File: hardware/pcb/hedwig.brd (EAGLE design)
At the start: 76.2 x 68.5 mm, 75 parts, among them IC1 MPL3115A2LGA, J1 DX07B024JJ1R1500, P1 JTAG-10MINI, Q1 16MHz, Q2 IRLML6402, U1 NRF24L01SMD, U2 TEXAS_INSTRUMENTS_TLC59731DRT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, U3 FT232RQ, U5 ADP2302, U7 9DoF IMU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

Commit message: updated schematic and pcb
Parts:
- removed U$6: DIODE, falcon:SMB
- removed U7: 9DoF IMU, SparkFun-Sensors:QFN24-3X3
- added 1.8V: TPB2,54, testpad:B2,54
- added C22: 47uF, SparkFun-Capacitors:0603@1
- added D3: SURS8360BT3G, falcon:SMB
- added Q3, Q6: 20V/0.2A/8MHz/1.2Ω/1Vth, SparkFun-DiscreteSemi:SOT-416FL
- added R11, R8: 5.1k, SparkFun-Resistors:0603
- added R12, R14: 2.49k, SparkFun-Resistors:0603
- added U4: TPS7A26-1.8, falcon:WSON
- added U6: 9DoF IMU, SparkFun-Sensors:QFN24-3X3
- C10, C11: value 1.5pF -> 0.1uF
- C14: value 2.2uF -> 0.1uF
- C17: value 100nF -> 0.1uF
- C18, C19, C20, C21: device SparkFun-Capacitors:0603 -> SparkFun-Capacitors:0603@1
- C8, C9: value 8.2pF -> 0.1uF
- moved C16 63.1 mm to (45.9, 58.3), turned to 270 degrees
- moved C20 51.4 mm to (3.00, 9.00), turned to 0 degrees
- moved 5V 30.2 mm to (23.0, 13.4)
- moved Q2 12.3 mm to (17.0, 14.0)
- moved R10 10.7 mm to (28.0, 15.0)
- moved C12 8.54 mm to (65.9, 45.8)
- moved C15 8.54 mm to (63.9, 51.3)
- moved IC1 8.54 mm to (71.5, 47.5)
- moved C21 8.45 mm to (3.00, 12.0)
- moved C5 8.32 mm to (24.1, 53.5)
- moved U$4 7.70 mm to (45.0, 16.0)
- moved R7 7.25 mm to (34.0, 8.00), turned to 90 degrees
- moved R5 7.00 mm to (29.6, 60.3)
- moved R6 7.00 mm to (31.8, 60.3)
- moved U5 5.91 mm to (36.0, 19.0)
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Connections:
- new net 1P8V: 1.8V.TP, C16.1, Q3.1, Q6.1, R12.2, R14.2, U4.1, U6.13, U6.22
- new net N$15: J1.B5, R8.2
- new net N$26: J1.A5, R11.2
- new net SENSOR_SCL_LV: Q6.2, R14.1, U6.23
- new net SENSOR_SDA_LV: Q3.2, R12.1, U6.24
- net +3V3: now also C22.1, U4.4, U4.6; no longer C16.1, U7.13, U7.22
- net +5V: now also D3.@2; no longer U$6.@2
- net ADSD_STUB: now also U6.9; no longer U7.9
- net GND: now also C22.2, R11.1, R8.1, U4.3, U4.5, U6.18, U6.20; no longer U7.18, U7.20
- net REGOUT: now also U6.10; no longer U7.10
- net SENSOR_SCL: now also Q6.3; no longer U7.23
- net SENSOR_SDA: now also Q3.3; no longer U7.24
- net USB_VCC: now also D3.@1; no longer U$6.@1
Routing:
- net 1P8V: track 0.00 -> 53.5 mm
- net SENSOR_SCL: track 47.6 -> 80.5 mm, vias 0 -> 2
- net +5V: track 72.1 -> 39.6 mm, vias 2 -> 0
- net SENSOR_SDA_LV: track 0.00 -> 29.0 mm
- net SENSOR_SCL_LV: track 0.00 -> 27.4 mm, vias 0 -> 2
- net SENSOR_SDA: track 50.4 -> 76.6 mm
- net N$15: track 0.00 -> 11.1 mm
- net N$25: track 28.1 -> 18.4 mm
- net N$26: track 0.00 -> 8.13 mm
- net GND: track 129.4 -> 137.1 mm, vias 50 -> 67
- net N$16: track 14.0 -> 21.0 mm
- net +3V3: track 65.7 -> 60.2 mm, vias 7 -> 9
- net N$23: track 5.08 -> 8.44 mm
- net N$22: track 12.5 -> 15.1 mm
- net N$21: track 12.5 -> 15.0 mm
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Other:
- board size 76.2 x 68.5 mm -> 78 x 70 mm
- board text added: "FALCON 1.1"

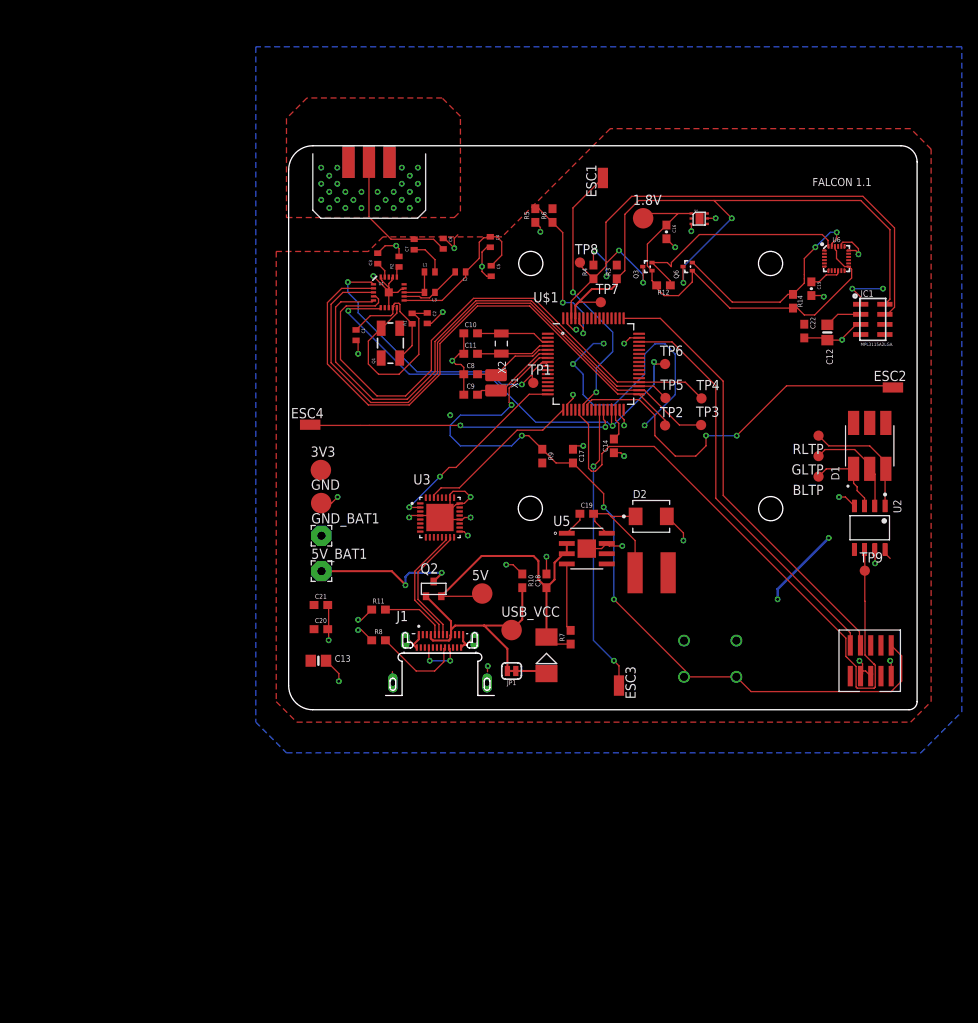
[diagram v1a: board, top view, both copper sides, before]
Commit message: change top plane to gnd and add breakout
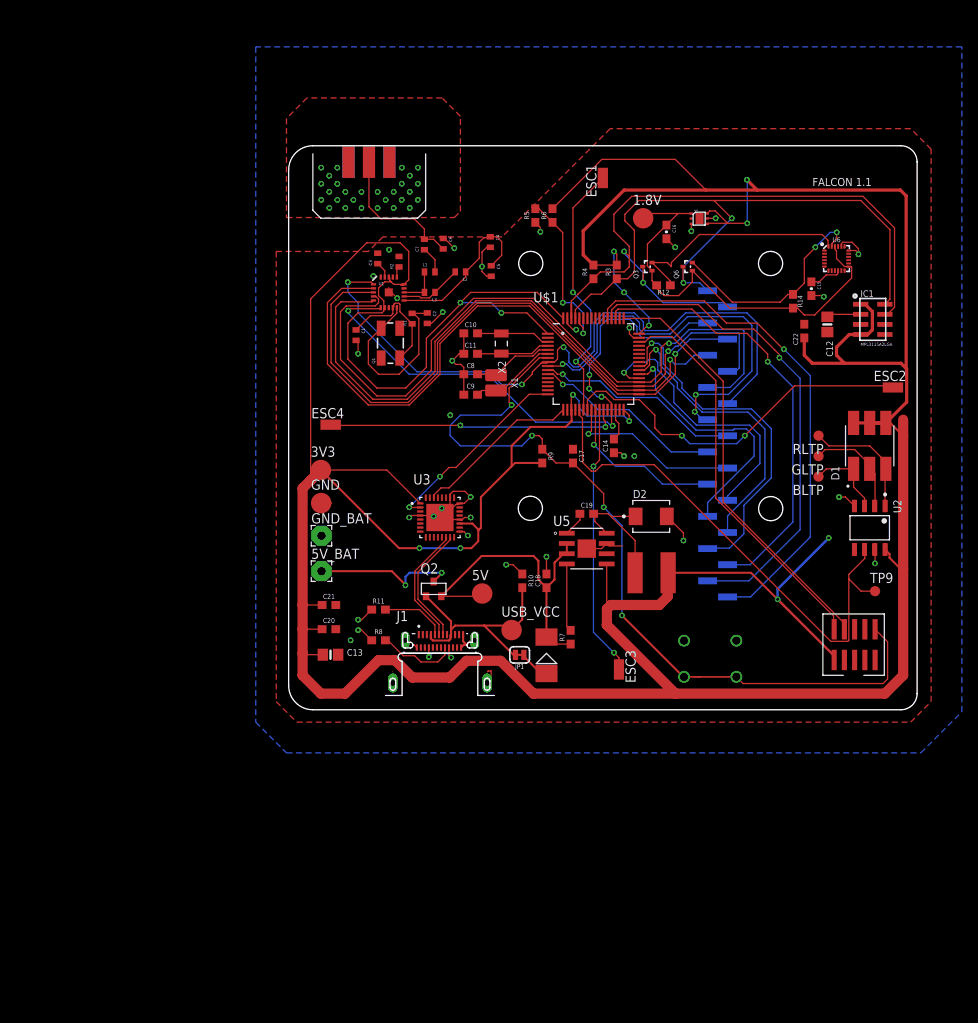
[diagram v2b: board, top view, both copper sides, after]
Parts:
- removed TP1, TP2, TP3, TP4, TP5, TP6, TP7, TP8: TPB1,27, testpad:B1,27
- added P2: SENSOR_SCL, falcon:STAGGERED-CONNECTOR
- added P3: RF_SCK, falcon:STAGGERED-CONNECTOR
- added P4: PC1, falcon:STAGGERED-CONNECTOR
- added P5: PC5, falcon:STAGGERED-CONNECTOR
- added P6: PC9, falcon:STAGGERED-CONNECTOR
- moved TP9 2.84 mm to (71.8, 13.7)
- moved P1 2.83 mm to (69.1, 7.08)
- moved ESC4 2.54 mm to (4.21, 34.4)
- moved JP1 2.24 mm to (27.7, 5.81)
- moved ESC3 2.00 mm to (40.0, 4.00)
- moved C13 1.68 mm to (4.19, 5.83)
- moved C7 1.27 mm to (15.8, 56.7)
- moved C12 1.00 mm to (65.9, 46.8)
- moved C20 1.00 mm to (4.00, 9.00)
- moved C21 1.00 mm to (4.00, 12.0)
- turned C22 to 90 degrees
- renumbered 5V_BAT1 to 5V_BAT, GND_BAT1 to GND_BAT
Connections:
- new net PC1: P4.1, U$1.9
- new net PC10: P6.2, U$1.51
- new net PC11: P6.3, U$1.52
- new net PC12: P6.4, U$1.53
- new net PC13: U$1.2
- new net PC2: P4.2, U$1.10
- new net PC3: P4.3, U$1.11
- new net PC4: P4.4, U$1.24
- new net PC5: P5.1, U$1.25
- new net PC6: P5.2, U$1.37
- new net PC7: P5.3, U$1.38
- new net PC8: P5.4, U$1.39
- new net PC9: P6.1, U$1.40
- net RF_CE: now also P3.4; no longer TP1.TP
- net RF_IRQ: now also P2.3; no longer TP6.TP
- net RF_MISO: now also P3.2; no longer TP5.TP
- net RF_MOSI: now also P3.3; no longer TP4.TP
- net RF_SCK: now also P3.1; no longer TP3.TP
- net RF_SS: now also P2.4; no longer TP2.TP
- net SENSOR_SCL: now also P2.1; no longer TP7.TP
- net SENSOR_SDA: now also P2.2; no longer TP8.TP
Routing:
- net +3V3: track 60.2 -> 579.1 mm, vias 9 -> 13
- net PC12: track 0.00 -> 64.0 mm, vias 0 -> 1
- net PC11: track 0.00 -> 61.8 mm, vias 0 -> 1
- net PC10: track 0.00 -> 54.6 mm, vias 0 -> 1
- net PC1: track 0.00 -> 51.7 mm, vias 0 -> 3
- net RF_CE: track 37.3 -> 84.5 mm, vias 2 -> 3
- net PC9: track 0.00 -> 44.4 mm, vias 0 -> 1
- net GND: track 137.1 -> 93.9 mm, vias 67 -> 61
- net PC8: track 0.00 -> 37.6 mm, vias 0 -> 1
- net PC6: track 0.00 -> 35.1 mm, vias 0 -> 1
- net PC7: track 0.00 -> 31.7 mm, vias 0 -> 1
- net PC2: track 0.00 -> 25.7 mm, vias 0 -> 1
- net PC3: track 0.00 -> 23.9 mm, vias 0 -> 1
- net PC4: track 0.00 -> 22.2 mm, vias 0 -> 1
- net PC5: track 0.00 -> 20.6 mm, vias 0 -> 1
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- removed copper zone on layer 1, net +3V3
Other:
- outline, holes or cut-outs redrawn
- board text added: "PC1"
- board text added: "PC11"
- board text added: "PC3"
- board text added: "PC5"
- board text added: "PC7"
- board text added: "PC9"
- board text added: "RF_IRQ"
- board text added: "RF_MOSI"
- board text added: "RF_SCK"
- board text added: "SENSOR_SCL"

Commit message: newest version - done
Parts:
- added C23: 47uF, SparkFun-Capacitors:0603@1
- added C24, C25: 0.1uF, SparkFun-Capacitors:0603@1
- added C26, C27, C28: 0.1uF, SparkFun-Capacitors:0603
- moved C13 73.1 mm to (68.7, 40.3), turned to 180 degrees
- moved C20 46.4 mm to (50.1, 14.4)
- moved C21 46.4 mm to (50.1, 17.4)
- moved C16 24.7 mm to (70.3, 54.9), turned to 90 degrees
- moved C22 16.2 mm to (52.1, 58.0), turned to 180 degrees
- moved C17 2.95 mm to (31.3, 30.4)
- moved R9 2.13 mm to (28.3, 30.5)
- moved ESC2 0.42 mm to (73.6, 39.1)
- renumbered IC1 to U7
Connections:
- removed net 1P8V: 1.8V.TP, C16.1, Q3.1, Q6.1, R12.2, R14.2, U4.1, U6.13, U6.22
- new net 1V8: 1.8V.TP, C16.1, C23.1, Q3.1, Q6.1, R12.2, R14.2, U4.1, U6.13, U6.22, U6.8
- net +3V3: now also C24.1, C25.1, C26.2, C27.2, C28.2
- net GND: now also C23.2, C24.2, C25.2, C26.1, C27.1, C28.1
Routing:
- net 1V8: track 0.00 -> 65.1 mm
- net 1P8V: track 53.7 -> 0.00 mm
- net GND: track 93.9 -> 86.2 mm, vias 61 -> 103
- net +3V3: track 579.1 -> 584.5 mm
- net SENSOR_SDA_LV: track 29.0 -> 28.3 mm
- net SWCLK: track 52.6 -> 53.2 mm
- net N$13: track 9.21 -> 9.81 mm
- net MOTOR2: track 46.3 -> 45.7 mm
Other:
- board text added: "/Users/adambujak/Workspace/FALCON/resources/tail.bmp"
- board text added: "PC10"
- board text added: "PC12"
- board text added: "PC2"
- board text added: "PC4"
- board text added: "PC6"
- board text added: "PC8"
- board text added: "RF_CE"
- board text added: "RF_MISO"
- board text added: "RF_SS"
- board text added: "SENSOR_SDA"
- board text removed: "FALCON 1.1"

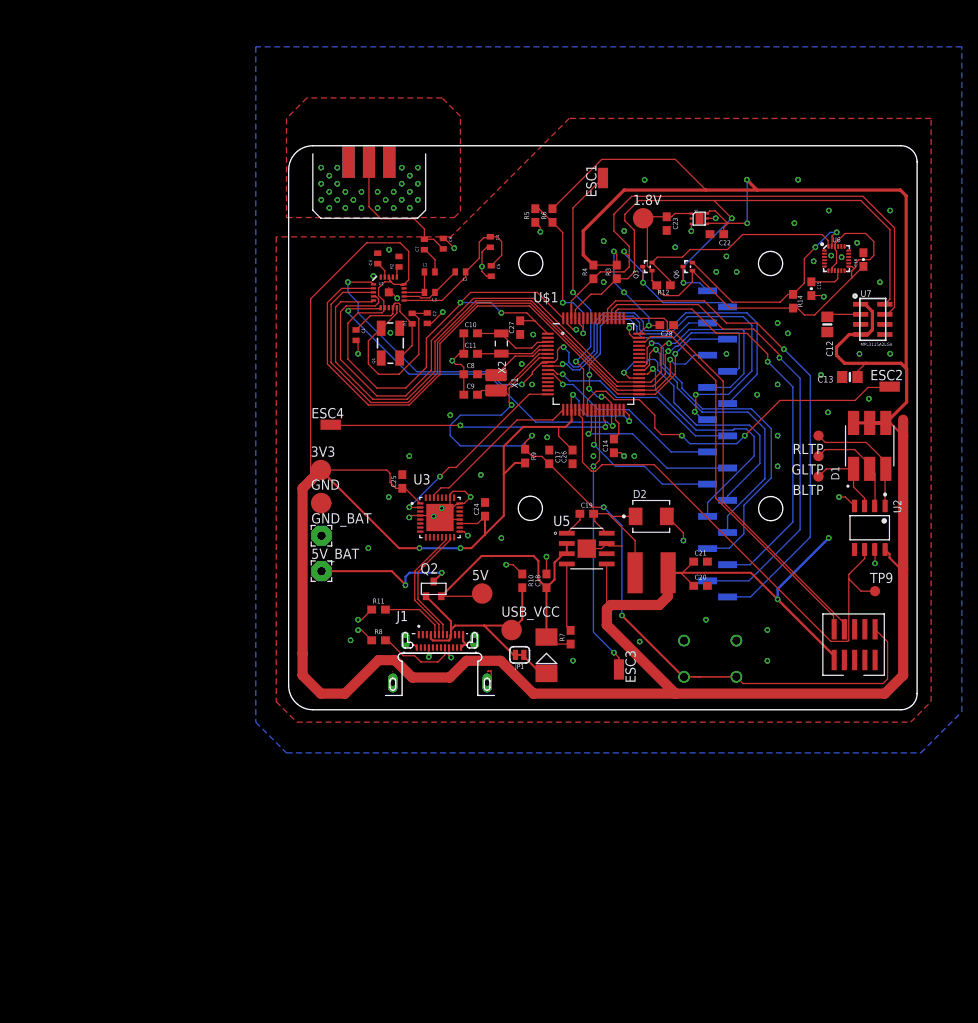
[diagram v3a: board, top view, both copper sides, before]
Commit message: Pcb overhall - put imu in middle, made board square
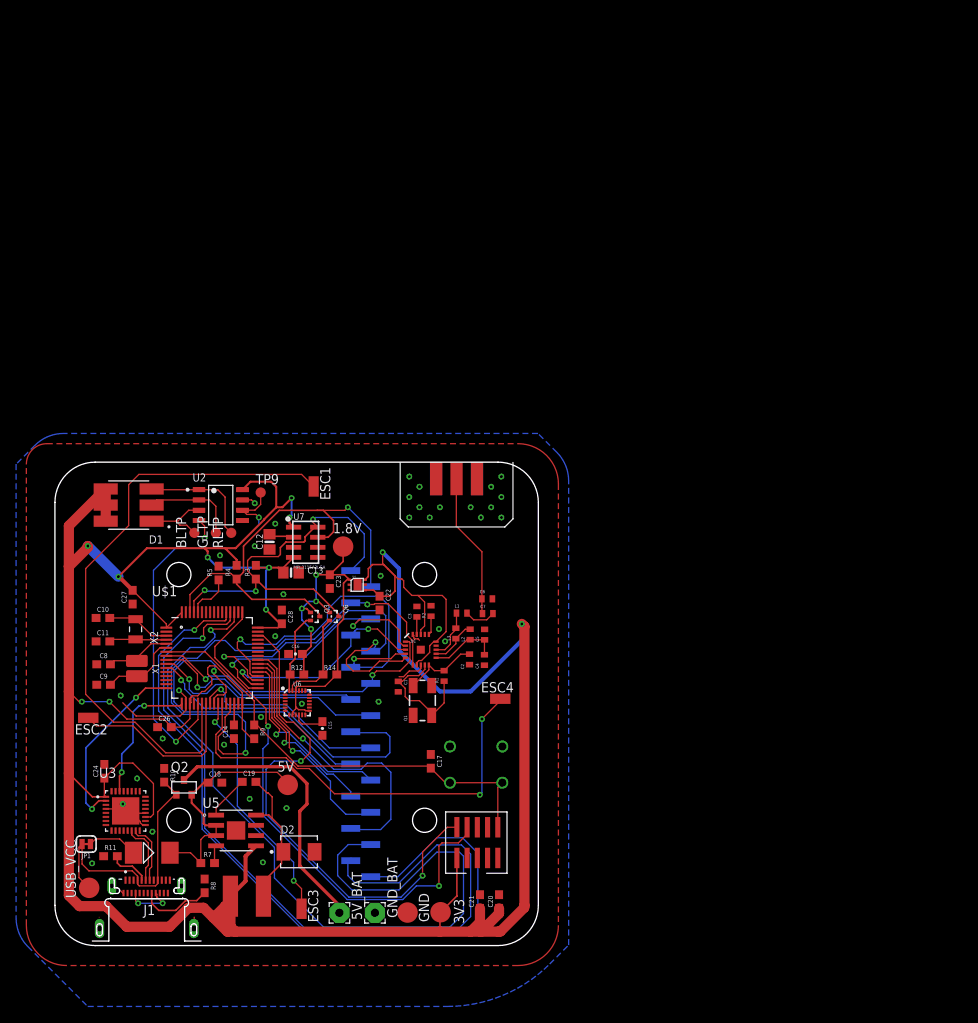
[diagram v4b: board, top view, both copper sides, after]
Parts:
- removed C25: 0.1uF, SparkFun-Capacitors:0603@1
- removed R6: 470, SparkFun-Resistors:0603
- moved ESC2 107.6 mm to (-25.9, -2.00), turned to 90 degrees
- moved D1 92.3 mm to (-20.9, 24.4), turned to 180 degrees
- moved U6 86.7 mm to (0.07, -0.13)
- moved C16 85.8 mm to (-0.16, 5.92), turned to 180 degrees
- moved C15 81.6 mm to (3.19, -3.32)
- moved U2 80.6 mm to (-9.43, 24.4), turned to 0 degrees
- moved BLTP 77.8 mm to (-12.7, 21.0), turned to 90 degrees
- moved TP9 77.2 mm to (-4.47, 26.0)
- moved U7 75.6 mm to (1.11, 19.8)
- moved GLTP 75.4 mm to (-10.0, 21.0), turned to 90 degrees
- moved C12 74.3 mm to (-3.37, 19.8)
- moved RLTP 73.9 mm to (-8.13, 21.0), turned to 90 degrees
- moved R14 73.8 mm to (4.12, 3.38), turned to 0 degrees
- moved C13 73.5 mm to (-0.70, 16.0), turned to 0 degrees
- moved R12 66.4 mm to (0.03, 3.38), turned to 0 degrees
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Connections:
- net +3V3: no longer C25.1, R6.2
- net GND: no longer C25.2
- net N$16: no longer R6.1
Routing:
- net +3V3: track 584.5 -> 408.2 mm, vias 13 -> 11
- net GND: track 86.2 -> 30.7 mm, vias 103 -> 38
- net RF_SCK: track 77.8 -> 27.7 mm, vias 1 -> 2
- net PC10: track 54.6 -> 103.9 mm
- net NRST: track 104.0 -> 55.9 mm, vias 4 -> 0
- net RF_SS: track 82.0 -> 34.6 mm, vias 1 -> 2
- net RF_CE: track 84.5 -> 37.5 mm, vias 3 -> 2
- net MOTOR1: track 32.4 -> 75.7 mm, vias 2 -> 0
- net RF_MOSI: track 90.8 -> 48.3 mm, vias 1 -> 2
- net PC11: track 61.8 -> 102.2 mm
- net RF_MISO: track 85.6 -> 48.9 mm, vias 1 -> 2
- net PC12: track 64.0 -> 99.8 mm
- net SENSOR_SCL: track 81.7 -> 51.3 mm, vias 2 -> 3
- net SENSOR_SDA: track 88.2 -> 58.7 mm, vias 2 -> 1
- net PC1: track 51.7 -> 26.7 mm, vias 3 -> 1
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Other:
- board size 78 x 70 mm -> 60 x 60 mm
